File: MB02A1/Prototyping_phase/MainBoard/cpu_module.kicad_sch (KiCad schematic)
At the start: 1 part, among them U8 NUCLEO-F446RE

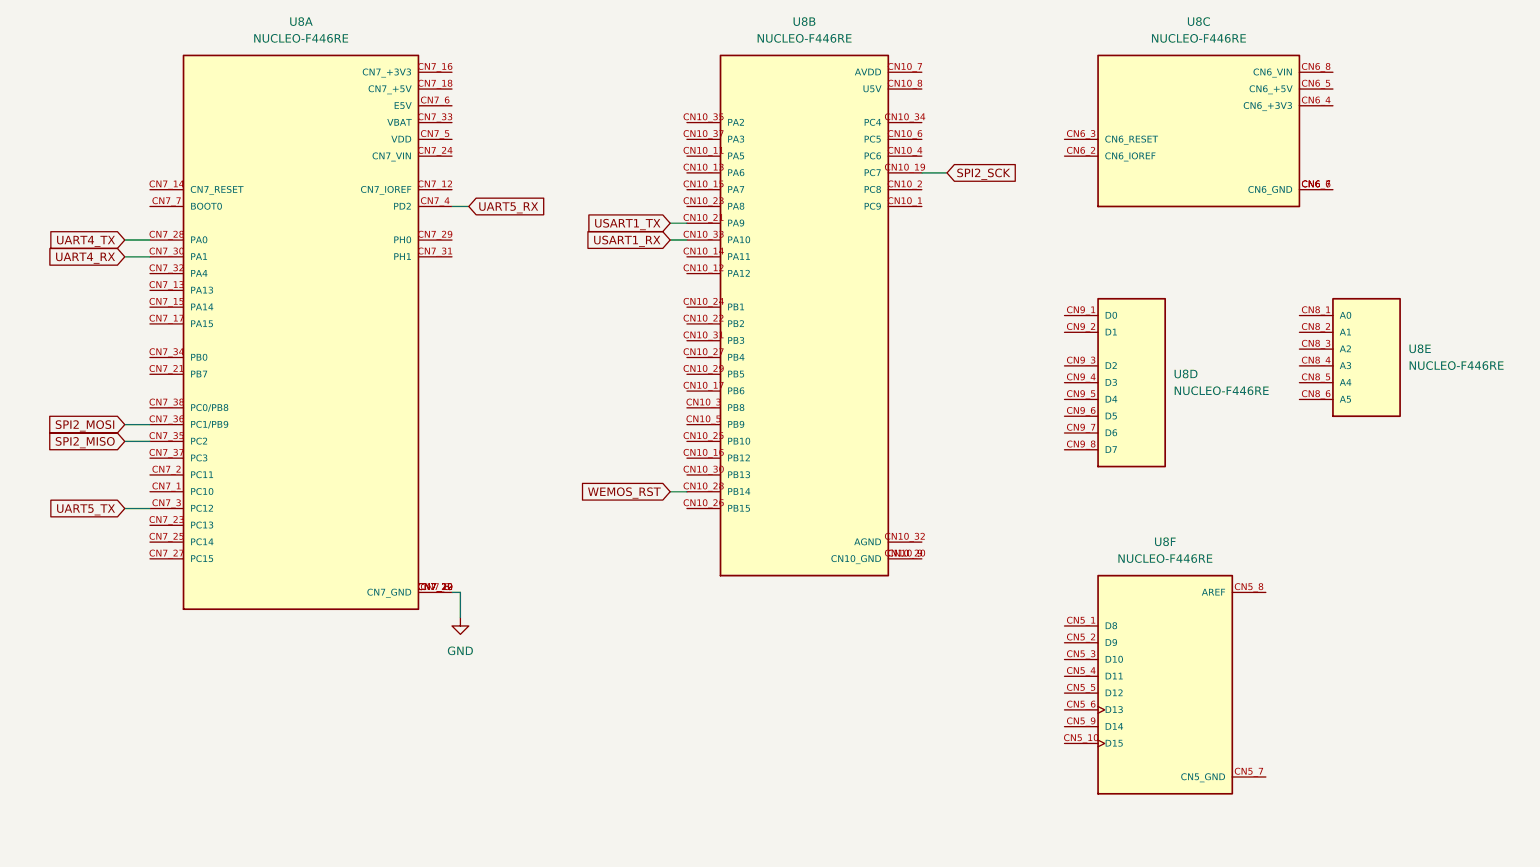
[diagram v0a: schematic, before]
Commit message: Datasheets added, design updated.
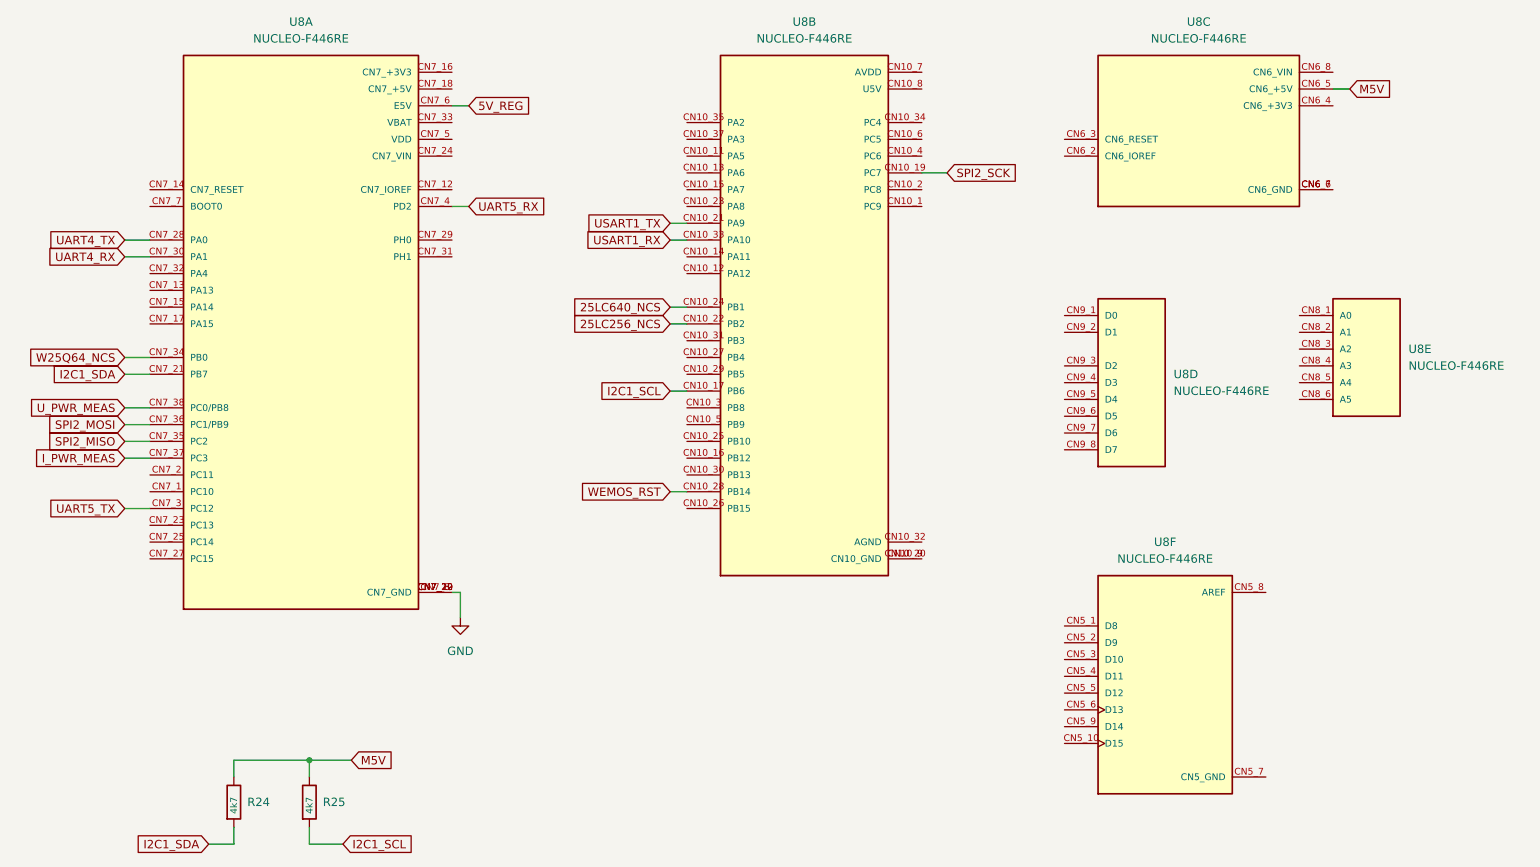
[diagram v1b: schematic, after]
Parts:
- added R24, R25: 4k7, Resistor_SMD:R_0805_2012Metric, symbol Device:R
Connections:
- net I2C1_SDA: now reaches U8.CN7_21 (PB7)
- net I2C1_SDA: now also R24.2
- net W25Q64_NCS: now reaches U8.CN7_34 (PB0)
- net I_PWR_MEAS: now reaches U8.CN7_37 (PC3)
- net U_PWR_MEAS: now reaches U8.CN7_38 (PC0/PB8)
- net 5V_REG: now reaches U8.CN7_6 (E5V)
- net M5V: now reaches U8.CN6_5 (CN6_+5V)
- net M5V: now also R24.1, R25.1
- net I2C1_SCL: now reaches U8.CN10_17 (PB6)
- net I2C1_SCL: now also R25.2
- net 25LC256_NCS: now reaches U8.CN10_22 (PB2)
- net 25LC640_NCS: now reaches U8.CN10_24 (PB1)

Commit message: Design update, production preparation.
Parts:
- renumbered R24 to R22, R25 to R23, U8 to U9
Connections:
- net DISPL_SCK: now reaches U9.CN7_1 (PC10)
- net DISPL_BNESS: now reaches U9.CN7_17 (PA15)
- net DISPL_MISO: now reaches U9.CN7_2 (PC11)
- net DAC_OUT: now reaches U9.CN7_32 (PA4)
- net M3V3: now reaches U9.CN6_4 (CN6_+3V3)
- net PWM3: now reaches U9.CN10_1 (PC9)
- net SPI2_CS0: now reaches U9.CN10_12 (PA12)
- net EXTI1: now reaches U9.CN10_13 (PA6)
- net PWM2: now reaches U9.CN10_14 (PA11)
- net EXTI2: now reaches U9.CN10_15 (PA7)
- net EXTI3: now reaches U9.CN10_2 (PC8)
- net PWM1: now reaches U9.CN10_23 (PA8)
- net DISPL_DC: now reaches U9.CN10_26 (PB15)
- net DISPL_RST: now reaches U9.CN10_27 (PB4)
- net DISPL_MOSI: now reaches U9.CN10_29 (PB5)
- net DISPL_TCH_CS: now reaches U9.CN10_3 (PB8)
- net DISPL_CS: now reaches U9.CN10_30 (PB13)
- net ADC1: now reaches U9.CN10_34 (PC4)
- net SPI2_CS1: now reaches U9.CN10_4 (PC6)
- net DISPL_TIRQ: now reaches U9.CN10_5 (PB9)
- net ADC2: now reaches U9.CN10_6 (PC5)
